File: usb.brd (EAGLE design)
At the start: 44.4 x 58.1 mm, 9 parts, among them J1 UJ31-CH-3-SMT-TR

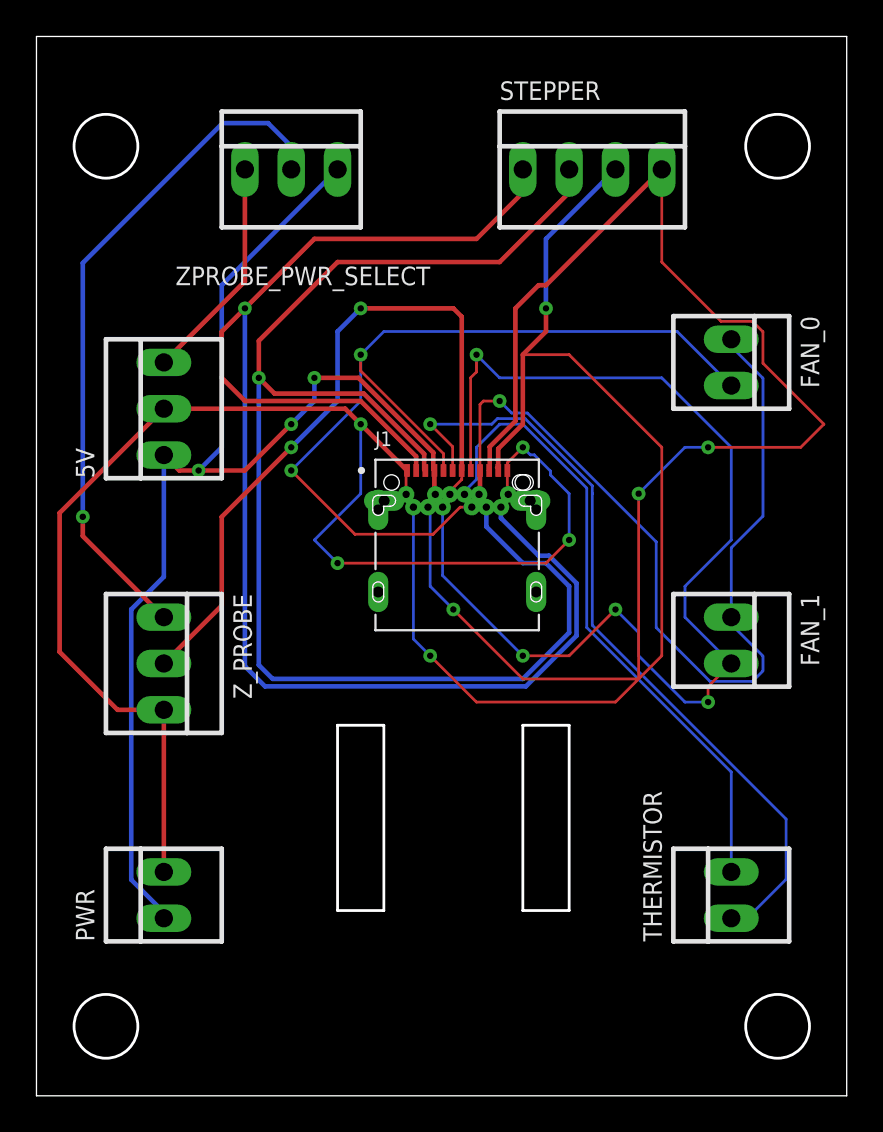
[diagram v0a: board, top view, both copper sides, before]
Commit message: Changed to vertical plug
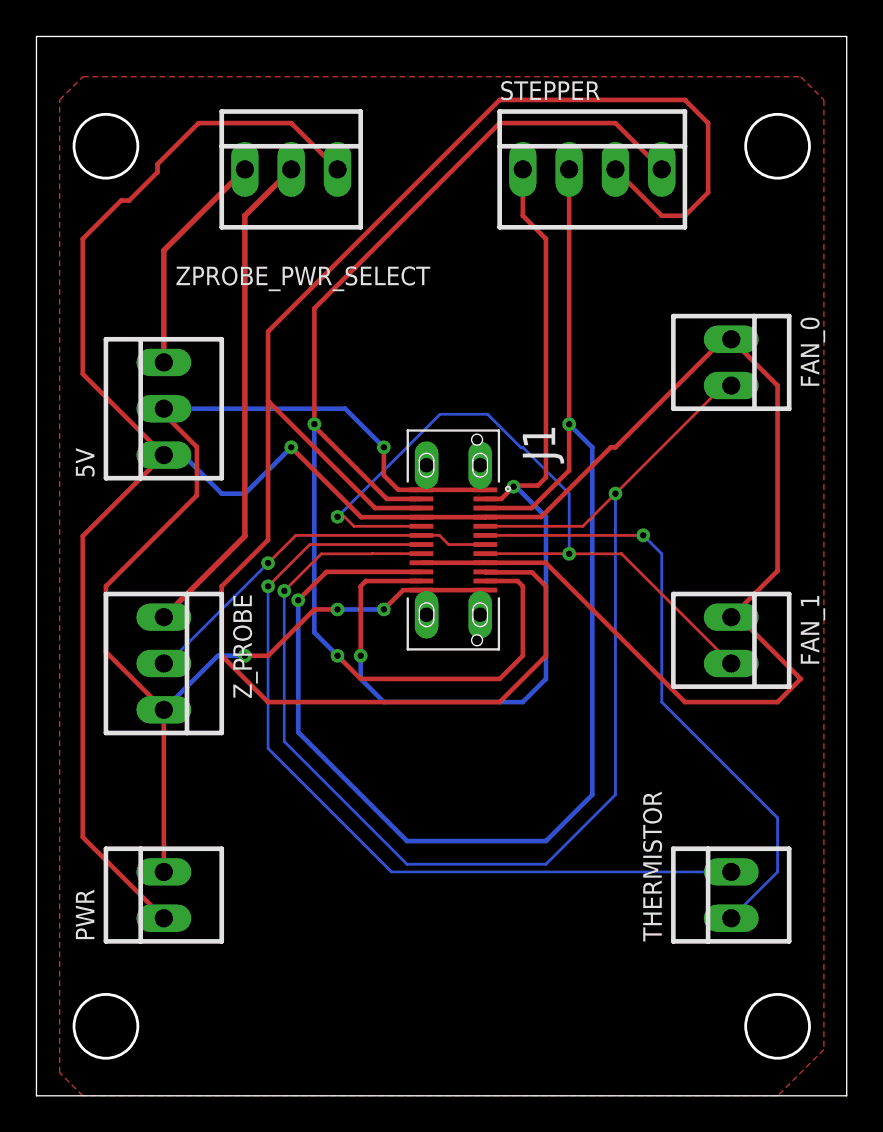
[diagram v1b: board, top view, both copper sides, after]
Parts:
- J1: value UJ31-CH-3-SMT-TR -> DX07S024WJ3R400; device UJ31-CH-3-SMT-TR:CUI_UJ31-CH-3-SMT-TR -> DX07S024WJ3R400:JAE_DX07S024WJ3R400
- moved J1 4.58 mm to (22.9, 30.5), turned to 270 degrees
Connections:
- removed net SHIELD: J1.SH1, J1.SH2, J1.SH3, J1.SH4, J1.SH5, J1.SH6
- net 2A: now also J1.A10, J1.B10; no longer J1.A11, J1.B11
- net 2B: now also J1.A11, J1.B11; no longer J1.A10, J1.B10
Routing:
- net 2A: track 63.5 -> 97.4 mm, vias 2 -> 0
- net 1A: track 85.2 -> 52.3 mm, vias 1 -> 2
- net VIN: track 118.8 -> 146.4 mm, vias 4 -> 1
- net FAN1: track 63.2 -> 40.9 mm, vias 4 -> 2
- net FAN0: track 50.2 -> 72.3 mm
- net ZPROBE: track 39.7 -> 20.7 mm, vias 2 -> 1
- net TH_B: track 35.2 -> 46.5 mm, vias 0 -> 1
- net 2B: track 79.2 -> 68.7 mm, vias 3 -> 2
- net Z_PWR: track 37.7 -> 27.4 mm, vias 1 -> 0
- net TH_A: track 43.5 -> 33.8 mm
- net GND: track 79.3 -> 70.2 mm
- net 1B: track 79.1 -> 77.1 mm, vias 1 -> 2
- added copper zone on layer 1, net GND
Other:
- outline, holes or cut-outs redrawn
